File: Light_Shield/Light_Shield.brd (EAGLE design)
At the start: 100 x 77.5 mm, 49 parts, among them Q1 BC846ASMD, Q2 BC846ASMD, U1 ARDUINO_SHIELDLABEL

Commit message: Further modifications to board opitmization.
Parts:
- moved R11 22.7 mm to (12.7, 44.5), turned to 90 degrees
- moved JP2 17.2 mm to (40.6, 72.4)
- moved JP4 17.2 mm to (23.5, 72.4)
- moved D3 16.6 mm to (21.6, 61.0)
- moved R1 13.5 mm to (33.7, 66.7)
- moved R21 11.8 mm to (11.4, 65.4), turned to 0 degrees
- moved Q2 11.0 mm to (18.4, 57.1)
- moved R3 11.0 mm to (15.9, 69.2)
- moved R6 10.3 mm to (23.5, 57.1), turned to 270 degrees
- moved R22 10.2 mm to (11.4, 60.3)
- moved R5 8.52 mm to (19.1, 64.1)
- moved R7 6.99 mm to (15.2, 64.1), turned to 0 degrees
- moved C1 6.38 mm to (26.0, 64.8)
- moved LED2 6.29 mm to (20.3, 66.7)
- moved R9 5.99 mm to (27.3, 67.9)
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
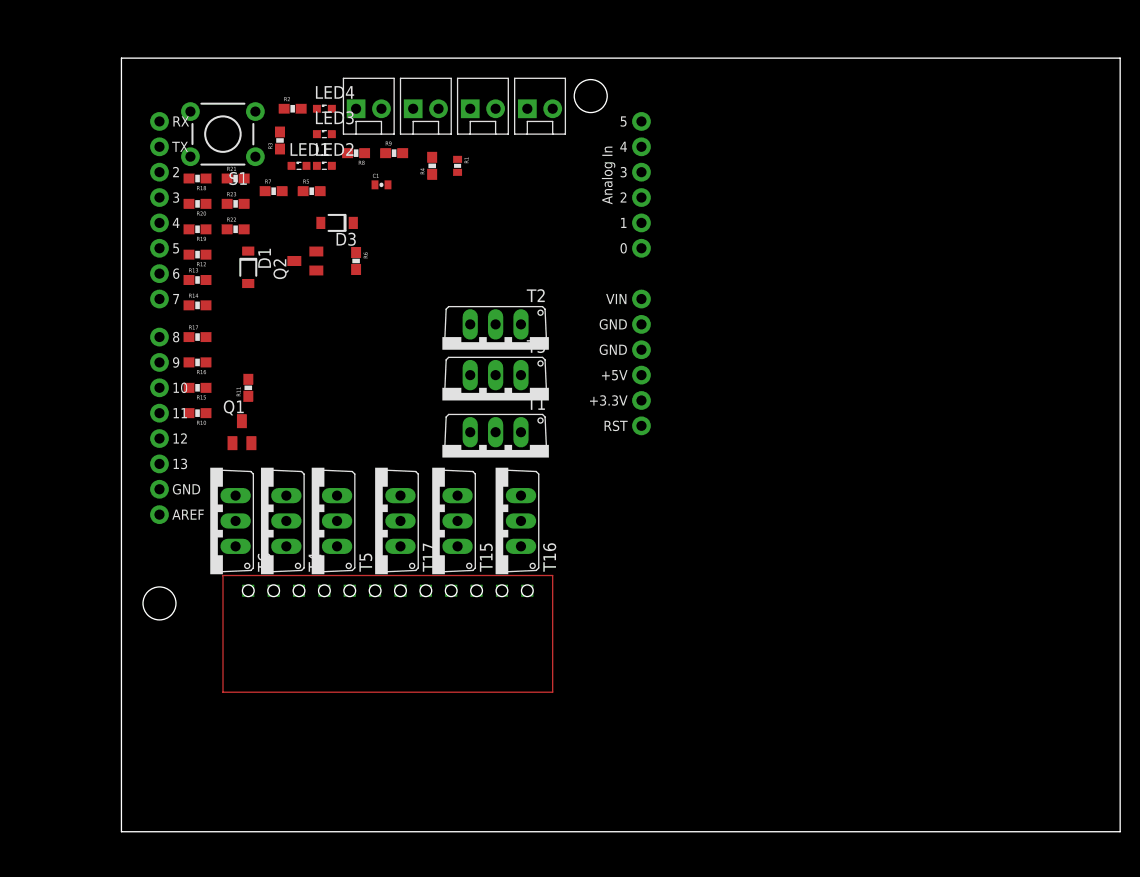
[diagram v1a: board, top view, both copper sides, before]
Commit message: Updated version of light shield with further placement optimizations
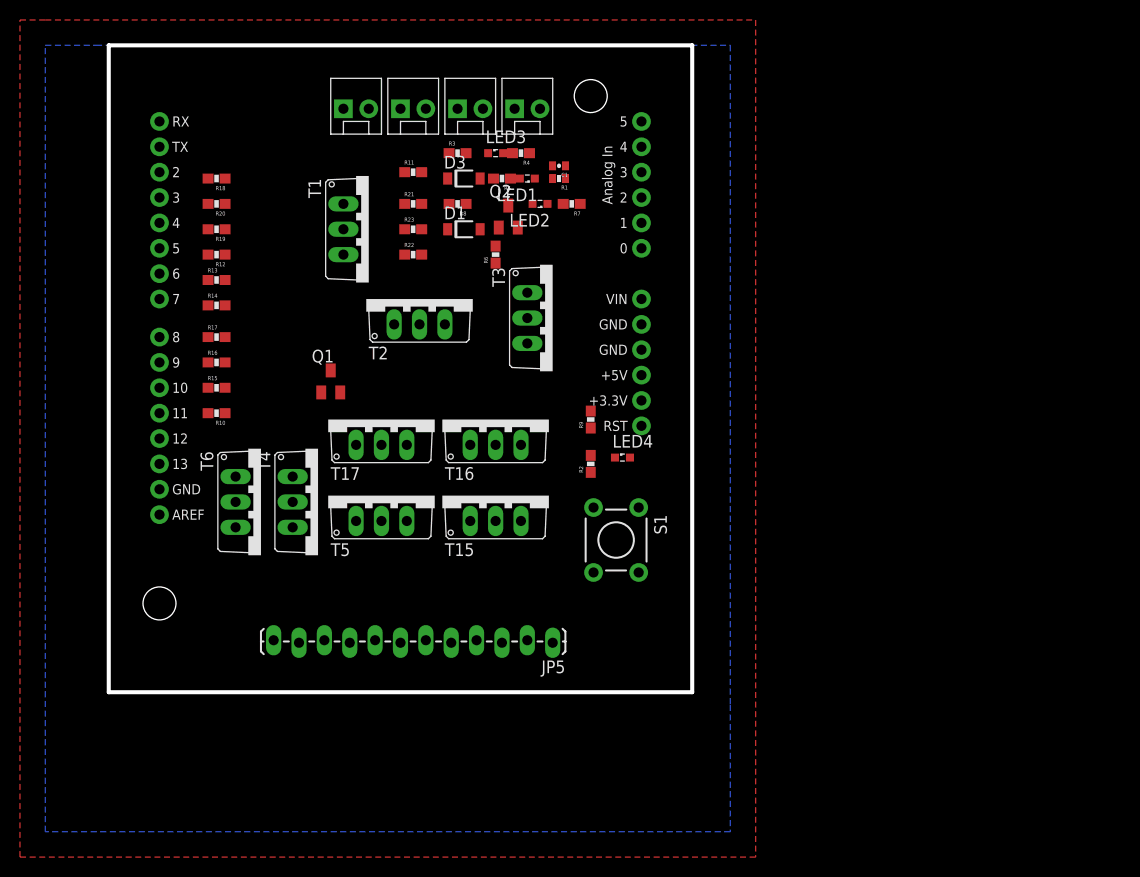
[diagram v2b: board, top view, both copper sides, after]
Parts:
- removed U$3: IGVC12PINCON, IGVC12PinCon:IGVC12PINPKG
- added JP5: M12LOCK_LONGPADS, SparkFun-Connectors:1X12_LOCK_LONGPADS
- moved S1 56.6 mm to (49.5, 29.2), turned to 270 degrees
- moved R2 46.4 mm to (47.0, 36.8), turned to 90 degrees
- moved LED4 45.9 mm to (50.2, 37.5)
- moved R9 33.1 mm to (47.0, 41.3), turned to 90 degrees
- moved R7 29.9 mm to (45.1, 62.9), turned to 180 degrees
- moved R11 27.2 mm to (29.2, 66.0), turned to 0 degrees
- moved T1 26.2 mm to (24.8, 60.3), turned to 270 degrees
- moved LED1 22.9 mm to (40.6, 65.4), turned to 180 degrees
- moved D1 21.9 mm to (34.3, 60.3), turned to 0 degrees
- moved LED2 21.9 mm to (41.9, 62.9), turned to 180 degrees
- moved Q2 20.8 mm to (38.7, 61.6), turned to 0 degrees
- moved R5 19.1 mm to (38.1, 65.4), turned to 180 degrees
- moved R21 18.0 mm to (29.2, 62.9)
- moved R22 18.0 mm to (29.2, 57.8)
- moved R23 18.0 mm to (29.2, 60.3)
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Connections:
- net 1S1_OUT: now also JP5.4; no longer U$3.S1
- net 1S2_OUT: now also JP5.5; no longer U$3.S2
- net 1S3_OUT: now also JP5.6; no longer U$3.S3
- net 2S1_OUT: now also JP5.10; no longer U$3.S4
- net 2S2_OUT: now also JP5.11; no longer U$3.S5
- net 2S3_OUT: now also JP5.12; no longer U$3.S6
- net BLUE_OUT: now also JP5.1; no longer U$3.BLUE
- net GREEN_OUT: now also JP5.2; no longer U$3.GREEN
- net RED_OUT: now also JP5.3; no longer U$3.RED
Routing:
- added copper zone on layer 1, net GND
- added copper zone on layer 16, net GND
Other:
- board size 100 x 77.5 mm -> 58.4 x 64.8 mm

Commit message: Final version of light shield; routed.
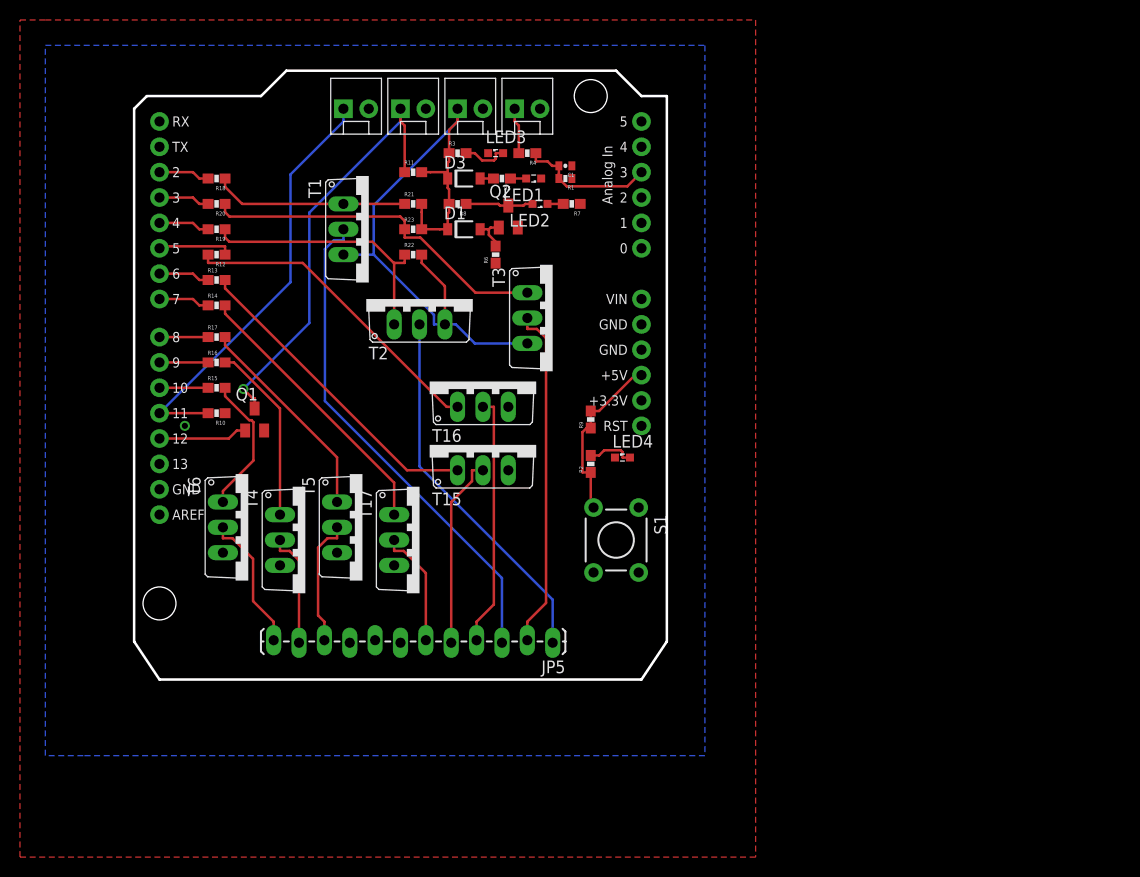
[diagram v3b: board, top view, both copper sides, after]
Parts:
- moved T17 12.7 mm to (29.8, 29.2), turned to 270 degrees
- moved Q1 8.52 mm to (13.3, 41.3)
- moved T15 5.24 mm to (36.2, 38.7)
- moved T16 4.02 mm to (36.2, 45.1)
- moved T4 4.02 mm to (18.4, 29.2)
- moved T5 3.70 mm to (24.1, 30.5), turned to 270 degrees
- moved T6 2.84 mm to (12.7, 30.5)
- moved C1 0.64 mm to (44.5, 66.7)
- moved R1 0.64 mm to (44.5, 65.4)
- moved LED1 0.63 mm to (41.3, 65.4)
- moved R4 0.63 mm to (40.6, 67.9)
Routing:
- net 12V: track 0.00 -> 69.0 mm
- net RED_OUT: track 0.00 -> 50.1 mm
- net N$6: track 0.00 -> 43.6 mm, vias 0 -> 1
- net SW_OFF: track 0.00 -> 43.0 mm
- net BLUE_OUT: track 0.00 -> 37.4 mm
- net N$19: track 0.00 -> 35.4 mm
- net GREEN_OUT: track 0.00 -> 34.4 mm
- net N$17: track 0.00 -> 31.8 mm
- net N$16: track 0.00 -> 31.7 mm
- net N$15: track 0.00 -> 28.0 mm
- net N$18: track 0.00 -> 26.8 mm
- net 1S1_OUT: track 0.00 -> 25.2 mm
- net N$11: track 0.00 -> 21.2 mm
- net N$9: track 0.00 -> 19.5 mm
- net 1S2_OUT: track 0.00 -> 19.2 mm
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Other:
- board size 58.4 x 64.8 mm -> 53.3 x 61 mm

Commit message: latest version
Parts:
- C1: value (none) -> 0.1uF
- R1: value (none) -> 536
- R2, R3, R5, R8, R9: value 200 -> 2700
- R4: value (none) -> 2700
- moved T15 22.6 mm to (20.7, 55.2)
- moved T2 17.2 mm to (46.5, 49.1), turned to 270 degrees
- moved T16 15.6 mm to (21.0, 48.6)
- moved T1 14.4 mm to (33.9, 49.1)
- moved T17 4.02 mm to (33.7, 30.5)
- moved T3 3.79 mm to (40.3, 49.0)
- moved T4 1.27 mm to (18.4, 30.5)
- moved T5 1.27 mm to (25.4, 30.5)
- moved T6 1.27 mm to (11.4, 30.5)
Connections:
- new net N$12: R9.1, S1.3, U1.RES
- net 12V: no longer D1.C, D3.C, R3.1, R8.2
- net 24V: now also D1.C, D3.C, R3.1, R8.2
- net 5V: no longer R9.1, S1.3
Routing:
- net N$18: track 26.8 -> 52.9 mm
- net N$16: track 31.7 -> 8.84 mm
- net 1S2_OUT: track 19.2 -> 39.9 mm
- net RED_OUT: track 50.1 -> 33.6 mm
- net 12V: track 69.0 -> 53.2 mm
- net 24V: track 4.62 -> 20.4 mm
- net N$12: track 0.00 -> 15.0 mm
- net N$9: track 19.5 -> 32.6 mm, vias 0 -> 1
- net N$17: track 31.8 -> 20.9 mm
- net 1S1_OUT: track 25.2 -> 33.6 mm
- net BLUE_OUT: track 37.4 -> 32.0 mm
- net 5V: track 17.9 -> 14.4 mm
- net GREEN_OUT: track 34.4 -> 31.6 mm
- net 1S3_OUT: track 11.9 -> 13.7 mm
- net N$15: track 28.0 -> 29.4 mm
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
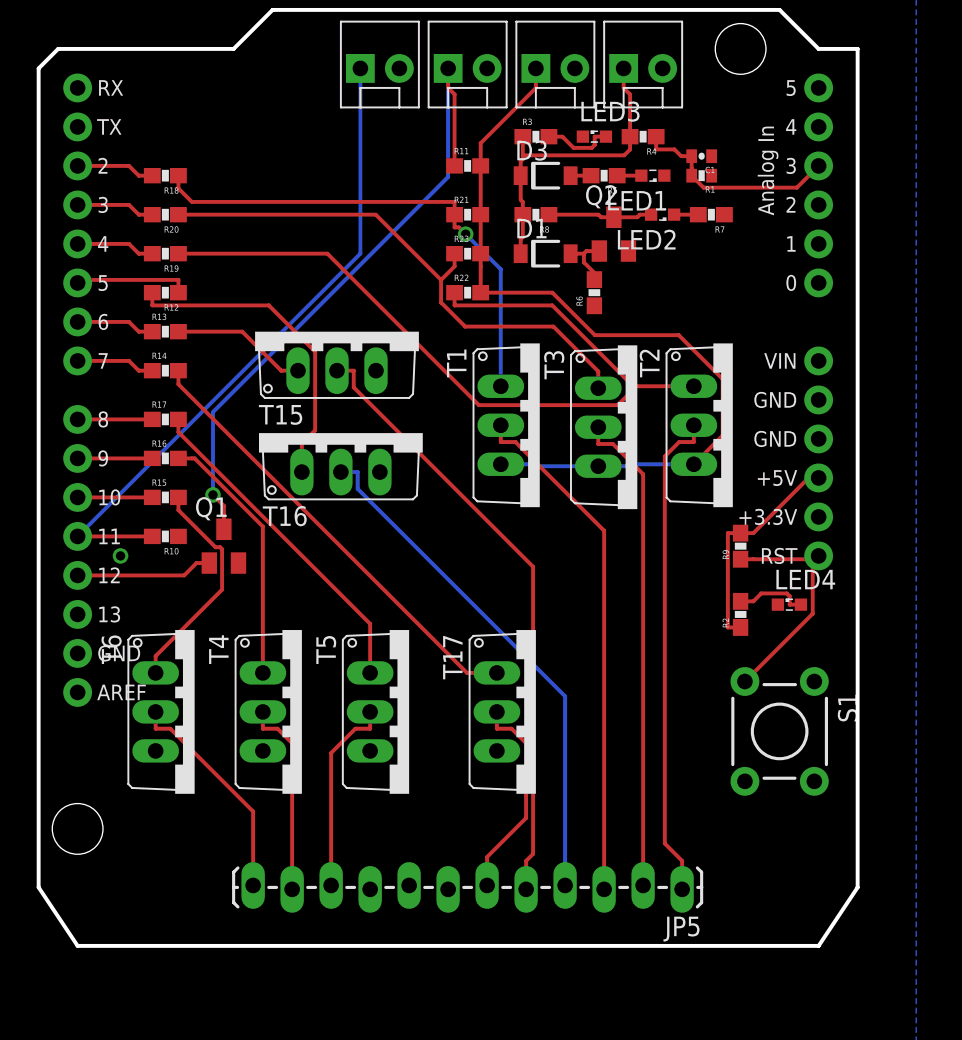
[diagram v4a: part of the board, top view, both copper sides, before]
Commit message: Fixes layout to ensure clustered LEDs and legible labels.
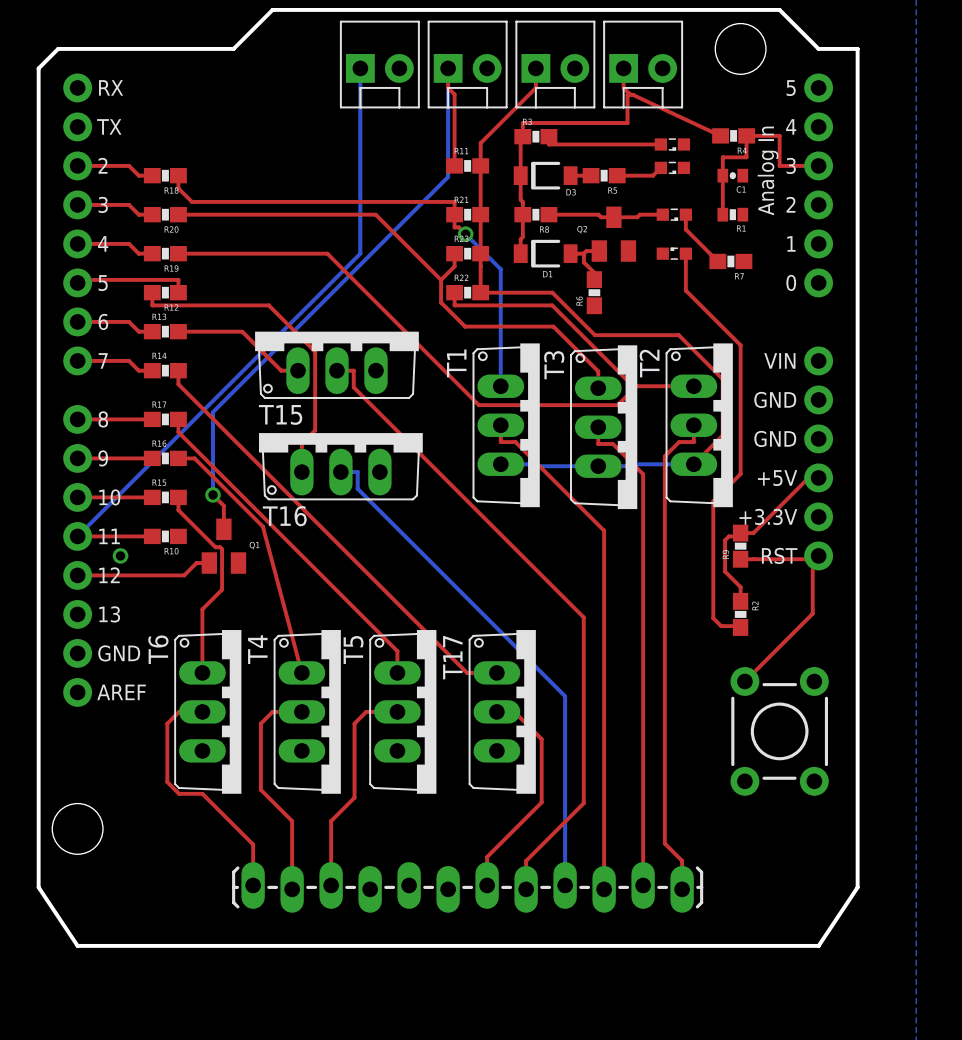
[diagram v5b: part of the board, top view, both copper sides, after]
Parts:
- JP5: value M12LOCK_LONGPADS -> Underglow
- LED1: value VOLTAGE_TOO_HIGH -> High
- LED2: value VOLTAGE_TOO_LOW -> Low
- LED3: value POWER_ON -> PWR
- LED4: value ARDUINO_ON -> USB
- moved LED4 24.1 mm to (42.7, 60.3)
- moved R4 5.89 mm to (46.5, 68.0)
- moved LED3 5.11 mm to (42.5, 67.4), turned to 180 degrees
- moved R7 3.30 mm to (46.4, 59.8)
- moved R1 3.25 mm to (46.5, 62.9)
- moved T6 3.05 mm to (14.5, 30.5)
- moved T4 2.54 mm to (21.0, 30.5)
- moved C1 2.40 mm to (46.5, 65.4)
- moved T5 1.78 mm to (27.2, 30.5)
- moved LED1 1.37 mm to (42.5, 65.9)
- moved LED2 0.76 mm to (42.7, 62.9)
- turned R2 to 270 degrees
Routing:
- net N$5: track 4.76 -> 28.0 mm
- net 24V: track 20.4 -> 26.1 mm
- net N$2: track 4.64 -> 7.80 mm
- net 1S2_OUT: track 39.9 -> 42.6 mm
- net N$10: track 1.58 -> 3.91 mm
- net 5V: track 14.4 -> 12.2 mm
- net 2S3_OUT: track 14.5 -> 16.3 mm
- net 2S2_OUT: track 12.9 -> 14.6 mm
- net N$8: track 1.57 -> 3.06 mm
- net 2S1_OUT: track 12.9 -> 14.3 mm
- net N$14: track 14.6 -> 13.3 mm
- net 1S3_OUT: track 13.7 -> 14.7 mm
- net N$3: track 6.80 -> 7.56 mm
- net N$11: track 21.7 -> 22.4 mm
